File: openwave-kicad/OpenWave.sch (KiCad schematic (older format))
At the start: 38 parts, among them IC1 STM32F405RGT, J1 USB_OTG, J2 503182-1852, SW1 SW_Push, Y1 8MHz, Y2 32.768KHz

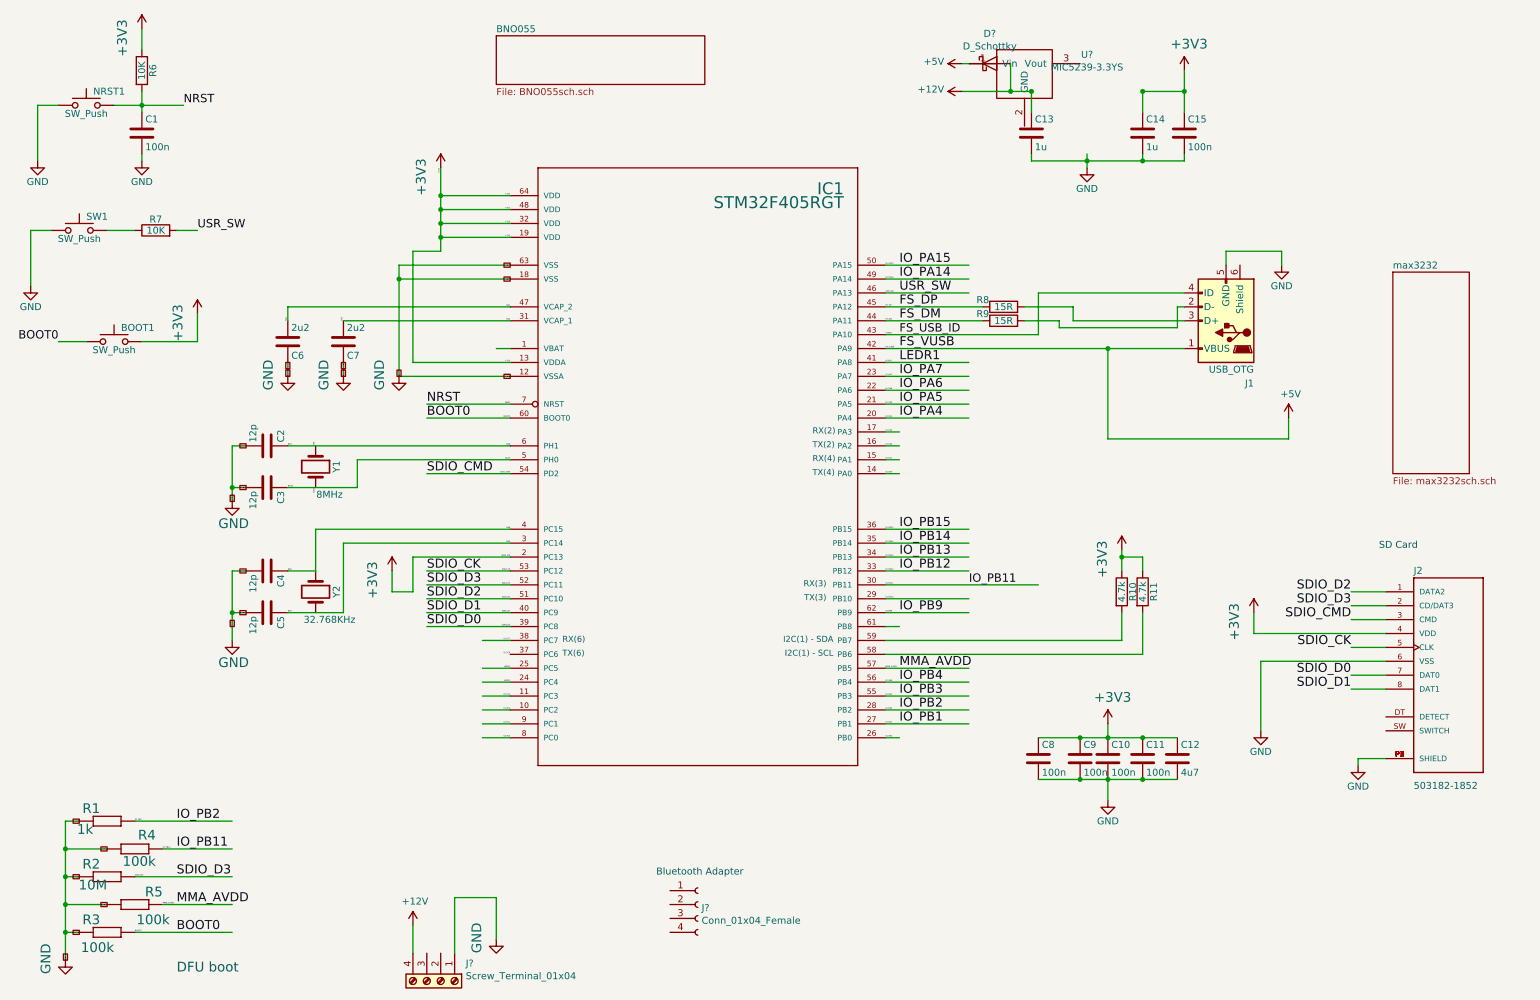
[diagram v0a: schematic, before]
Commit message: finished max232 schematic
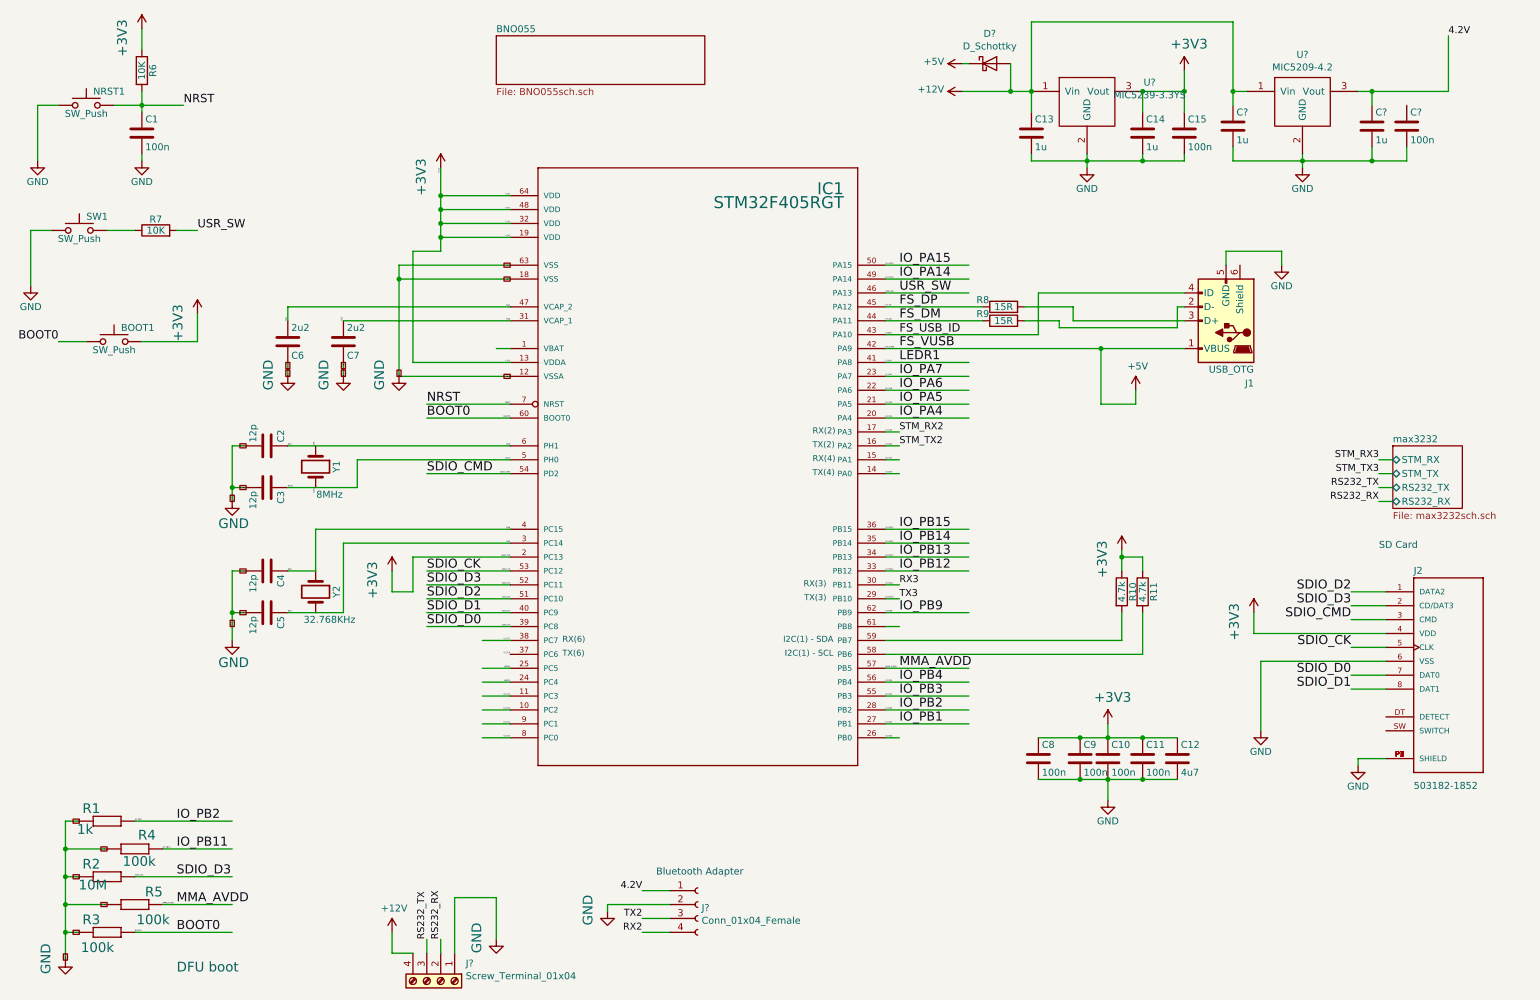
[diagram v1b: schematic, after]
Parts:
- added C? (x2): 1u, Capacitors_SMD:C_0603, symbol Device:C
- added C?: 100n, Capacitors_SMD:C_0603, symbol Device:C
- added U?: MIC5209-4.2, symbol wattnotions:MIC5209-4.2
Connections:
- net labels added: 4.2V, RS232_RX, RS232_TX, RX2, RX3, STM_RX2, STM_RX3, STM_TX2, STM_TX3, TX2, TX3
- wire segments 188 -> 217
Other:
- moved on the sheet: U?
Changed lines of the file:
@@
 	1    0    0    -1
 $EndComp
-Text Label 7300 4650 0    60   ~ 0
-IO_PB11
 $Comp
 L wattnotions:503182-1852 J2
@@
 	3800 5650 4000 5650
 Wire Wire Line
-	6700 4750 7300 4750
-Wire Wire Line
-	6700 4650 7800 4650
-Wire Wire Line
 	3800 5750 4000 5750
 Wire Wire Line
@@
 Wire Wire Line
 	7800 2550 8850 2550
-Wire Wire Line
-	6700 2950 8300 2950
 Wire Wire Line
 	9150 2350 9150 2250
@@
 L power:+5V #PWR?
 U 1 1 5CA98EDB
-P 9600 3450
-F 0 "#PWR?" H 9600 3300 50  0001 C CNN
-F 1 "+5V" H 9615 3623 50  0000 C CNN
-F 2 "" H 9600 3450 50  0001 C CNN
-F 3 "" H 9600 3450 50  0001 C CNN
-	1    9600 3450
-	1    0    0    -1
-$EndComp
-Wire Wire Line
-	8300 2950 8300 3600
-Wire Wire Line
-	8300 3600 9600 3600
-Wire Wire Line
-	9600 3600 9600 3450
-Connection ~ 8300 2950
-Wire Wire Line
-	8300 2950 8850 2950
+P 8500 3250
+F 0 "#PWR?" H 8500 3100 50  0001 C CNN
+F 1 "+5V" H 8515 3423 50  0000 C CNN
+F 2 "" H 8500 3250 50  0001 C CNN
+F 3 "" H 8500 3250 50  0001 C CNN
+	1    8500 3250
+	1    0    0    -1
+$EndComp
 $Comp
 L wattnotions:MIC5239-3.3YS U?
 U 1 1 5CAAC9EC
-P 8150 1000
-F 0 "U?" H 8150 1165 50  0000 C CNN
-F 1 "MIC5239-3.3YS" H 8150 1074 50  0000 C CNN
-F 2 "" H 8150 950 50  0001 C CNN
-F 3 "" H 8150 950 50  0001 C CNN
-	1    8150 1000
+P 8600 1200
+F 0 "U?" H 8600 1365 50  0000 C CNN
+F 1 "MIC5239-3.3YS" H 8600 1274 50  0000 C CNN
+F 2 "" H 8600 1150 50  0001 C CNN
+F 3 "" H 8600 1150 50  0001 C CNN
+	1    8600 1200
 	1    0    0    -1
 $EndComp
@@
 L power:+12V #PWR?
 U 1 1 5CB01041
-P 3300 7100
-F 0 "#PWR?" H 3300 6950 50  0001 C CNN
-F 1 "+12V" H 3315 7273 50  0000 C CNN
-F 2 "" H 3300 7100 50  0001 C CNN
-F 3 "" H 3300 7100 50  0001 C CNN
-	1    3300 7100
+P 3150 7150
+F 0 "#PWR?" H 3150 7000 50  0001 C CNN
+F 1 "+12V" H 3165 7323 50  0000 C CNN
+F 2 "" H 3150 7150 50  0001 C CNN
+F 3 "" H 3150 7150 50  0001 C CNN
+	1    3150 7150
 	1    0    0    -1
 $EndComp
@@
 Wire Wire Line
 	3900 6900 3900 7200
-Wire Wire Line
-	3300 7300 3300 7100
-$Sheet
-S 10350 2400 550  1450
-U 5CB14458
-F0 "max3232" 50
-F1 "max3232sch.sch" 50
-$EndSheet
 Connection ~ 8100 5750
 Wire Wire Line
@@
 Wire Wire Line
 	7250 1100 7600 1100
+$Comp
+L wattnotions:MIC5209-4.2 U?
+U 1 1 5CB69853
+P 9700 1150
+F 0 "U?" H 9700 1465 50  0000 C CNN
+F 1 "MIC5209-4.2" H 9700 1374 50  0000 C CNN
+F 2 "" H 9700 1150 50  0001 C CNN
+F 3 "" H 9700 1150 50  0001 C CNN
+	1    9700 1150
+	1    0    0    -1
+$EndComp
+Wire Wire Line
+	7750 1100 7750 600
+Wire Wire Line
+	7750 600  9200 600
+Wire Wire Line
+	9200 600  9200 1100
+Wire Wire Line
+	9200 1100 9300 1100
+$Comp
+L power:GND #PWR?
+U 1 1 5CB73D5D
+P 9700 1650
+F 0 "#PWR?" H 9700 1400 50  0001 C CNN
+F 1 "GND" H 9700 1500 50  0000 C CNN
+F 2 "" H 9700 1650 50  0001 C CNN
+F 3 "" H 9700 1650 50  0001 C CNN
+	1    9700 1650
+	1    0    0    -1
+$EndComp
+Wire Wire Line
+	9700 1550 9700 1600
+$Comp
+L Device:C C?
+U 1 1 5CB7E204
+P 10200 1350
+F 0 "C?" H 10225 1450 50  0000 L CNN
+F 1 "1u" H 10225 1250 50  0000 L CNN
+F 2 "Capacitors_SMD:C_0603" H 10238 1200 50  0001 C CNN
+F 3 "" H 10200 1350 50  0001 C CNN
+	1    10200 1350
+	1    0    0    -1
+$EndComp
+$Comp
+L Device:C C?
+U 1 1 5CB7E28A
+P 10450 1350
+F 0 "C?" H 10475 1450 50  0000 L CNN
+F 1 "100n" H 10475 1250 50  0000 L CNN
+F 2 "Capacitors_SMD:C_0603" H 10488 1200 50  0001 C CNN
+F 3 "" H 10450 1350 50  0001 C CNN
+	1    10450 1350
+	1    0    0    -1
+$EndComp
+Wire Wire Line
+	10100 1100 10200 1100
+Wire Wire Line
+	10200 1100 10200 1200
+Connection ~ 10200 1100
+Wire Wire Line
+	10200 1100 10750 1100
+Wire Wire Line
+	10200 1500 10200 1600
+Wire Wire Line
+	10200 1600 9700 1600
+Connection ~ 9700 1600
+Wire Wire Line
+	9700 1600 9700 1650
+Wire Wire Line
+	10450 1500 10450 1600
+Wire Wire Line
+	10450 1600 10200 1600
+Connection ~ 10200 1600
+Text Label 10750 700  0    50   ~ 0
+4.2V
+Wire Wire Line
+	10750 700  10750 1100
+$Comp
+L Device:C C?
+U 1 1 5CBB4DA7
+P 9200 1350
+F 0 "C?" H 9225 1450 50  0000 L CNN
+F 1 "1u" H 9225 1250 50  0000 L CNN
+F 2 "Capacitors_SMD:C_0603" H 9238 1200 50  0001 C CNN
+F 3 "" H 9200 1350 50  0001 C CNN
+	1    9200 1350
+	1    0    0    -1
+$EndComp
+Wire Wire Line
+	9200 1100 9200 1200
+Connection ~ 9200 1100
+Wire Wire Line
+	9200 1500 9200 1600
+Wire Wire Line
+	9200 1600 9700 1600
+Text Label 4950 6850 2    50   ~ 0
+4.2V
+Wire Wire Line
+	5150 6850 4950 6850
+Wire Wire Line
+	5150 6950 4700 6950
+Wire Wire Line
+	4700 6950 4700 7000
+$Comp
+L power:GND #GND?
+U 1 1 5CBE31E3
+P 4700 7000
+F 0 "#GND?" H 4600 6900 70  0001 L BNN
+F 1 "GND" V 4600 6900 70  0000 L BNN
+F 2 "" H 4700 7000 60  0001 C CNN
+F 3 "" H 4700 7000 60  0001 C CNN
+	1    4700 7000
+	1    0    0    -1
+$EndComp
+Text Label 6800 3550 0    50   ~ 0
+STM_RX2
+Text Label 6800 3650 0    50   ~ 0
+STM_TX2
+Text Label 4950 7150 2    50   ~ 0
+RX2
+Text Label 4950 7050 2    50   ~ 0
+TX2
+Wire Wire Line
+	4950 7050 5150 7050
+Wire Wire Line
+	4950 7150 5150 7150
+Wire Wire Line
+	6700 2950 8250 2950
+Wire Wire Line
+	8250 2950 8250 3350
+Wire Wire Line
+	8250 3350 8500 3350
+Wire Wire Line
+	8500 3350 8500 3250
+Connection ~ 8250 2950
+Wire Wire Line
+	8250 2950 8850 2950
+Wire Wire Line
+	6700 4750 6800 4750
+Wire Wire Line
+	6700 4650 6800 4650
+Text Label 6800 4650 0    50   ~ 0
+RX3
+Text Label 6800 4750 0    50   ~ 0
+TX3
+Wire Wire Line
+	10350 3750 10250 3750
+Wire Wire Line
+	10350 3850 10250 3850
+Text Label 10250 3750 2    50   ~ 0
+STM_RX3
+Text Label 10250 3850 2    50   ~ 0
+STM_TX3
+$Sheet
+S 10350 3650 500  450
+U 5CB14458
+F0 "max3232" 50
+F1 "max3232sch.sch" 50
+F2 "STM_RX" B L 10350 3750 50
+F3 "STM_TX" B L 10350 3850 50
+F4 "RS232_TX" B L 10350 3950 50
+F5 "RS232_RX" B L 10350 4050 50
+$EndSheet
+Wire Wire Line
+	10350 3950 10250 3950
+Wire Wire Line
+	10350 4050 10250 4050
+Text Label 10250 3950 2    50   ~ 0
+RS232_TX
+Text Label 10250 4050 2    50   ~ 0
+RS232_RX
+Text Label 3400 7200 1    50   ~ 0
+RS232_TX
+Text Label 3500 7200 1    50   ~ 0
+RS232_RX
+Wire Wire Line
+	3300 7300 3150 7300
+Wire Wire Line
+	3150 7300 3150 7150
+Wire Wire Line
+	3400 7300 3400 7200
+Wire Wire Line
+	3500 7300 3500 7200
 $EndSCHEMATC

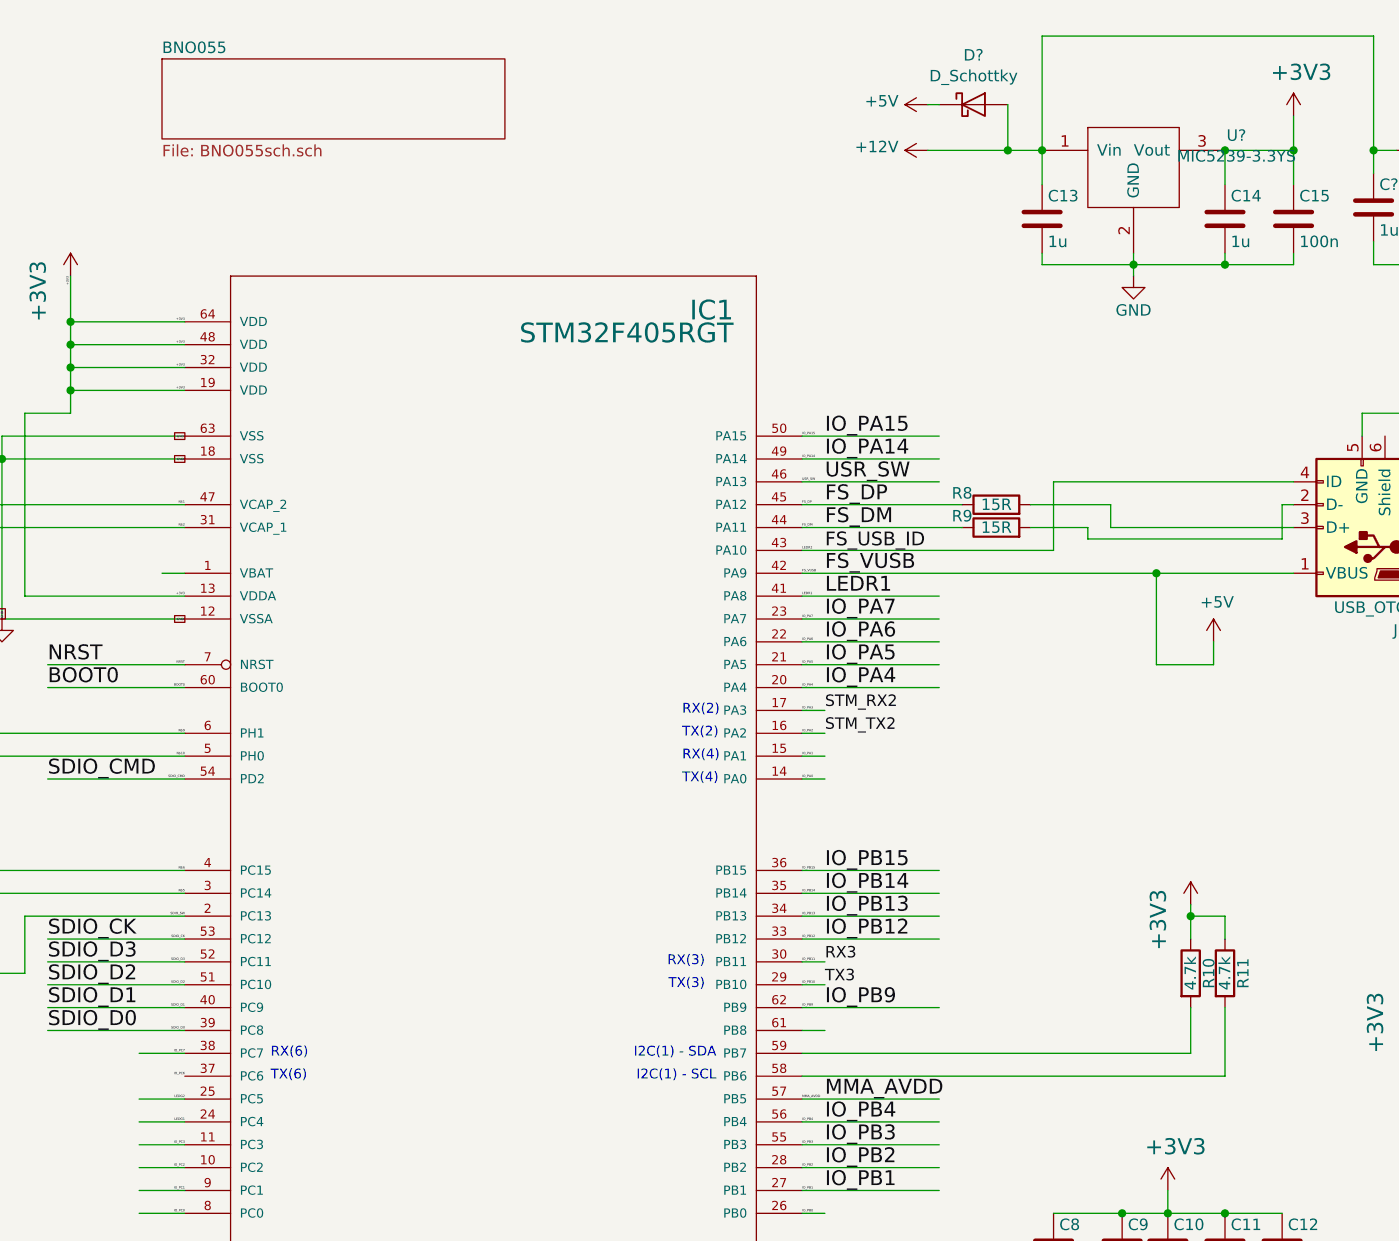
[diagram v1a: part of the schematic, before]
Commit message: finished bno055 schematic
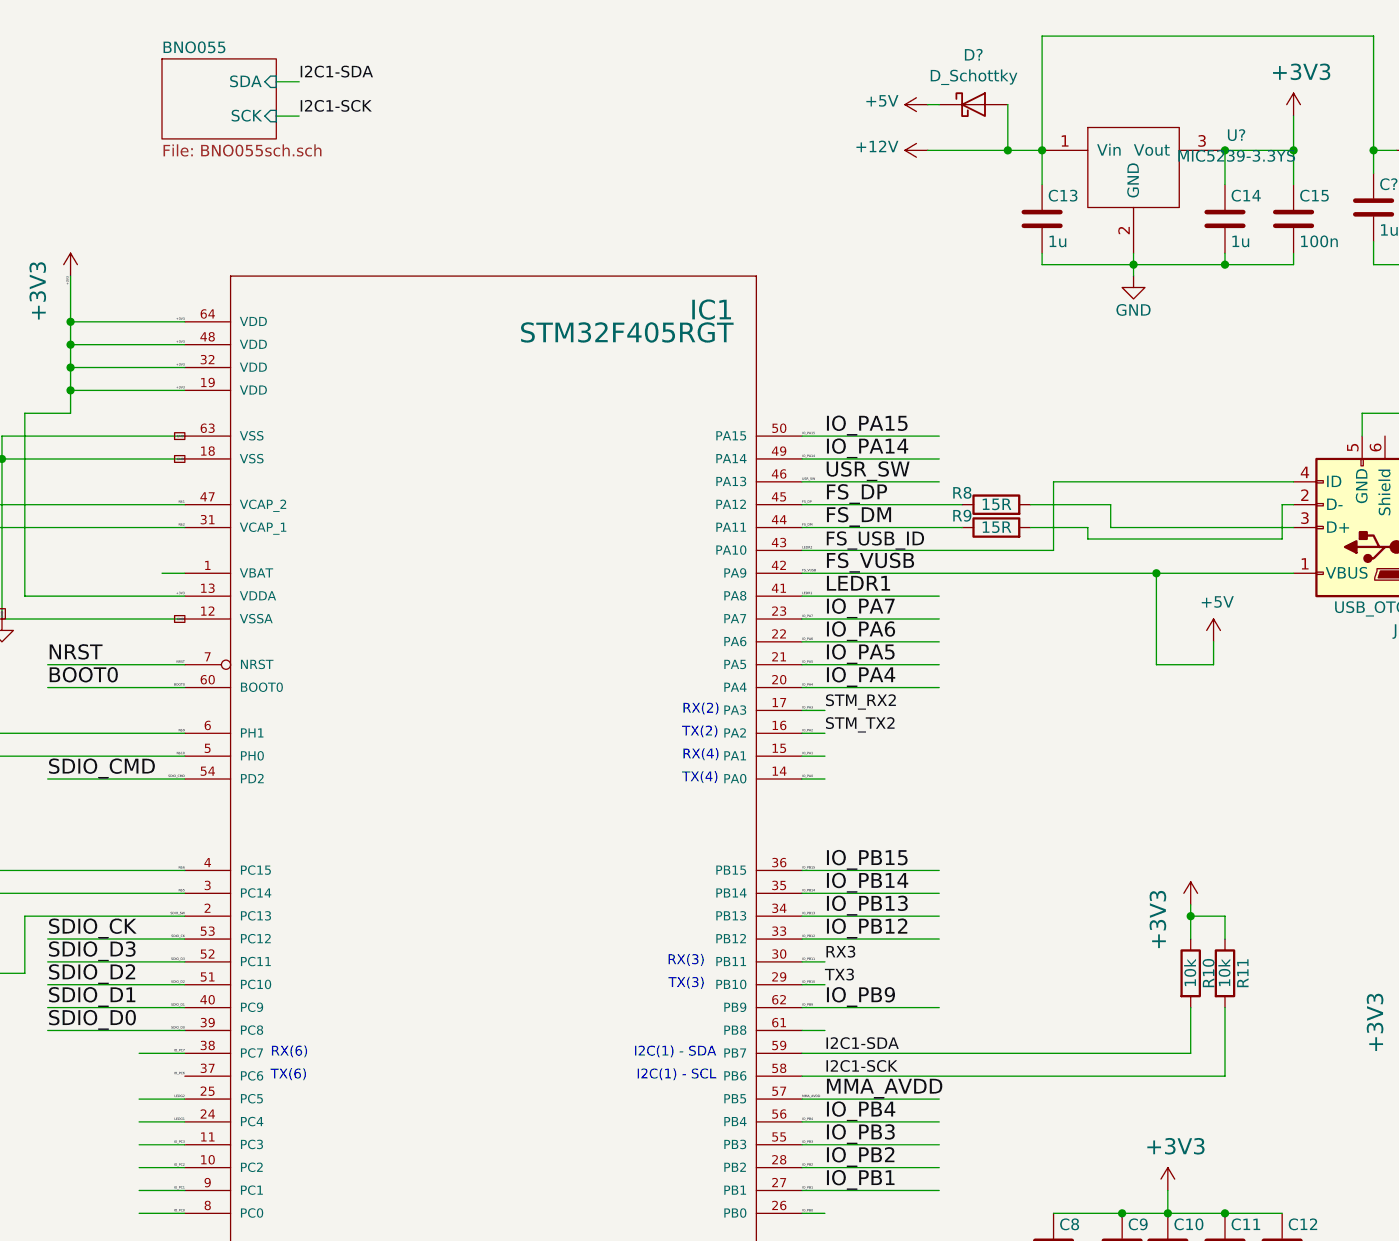
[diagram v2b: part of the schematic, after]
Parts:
- R10, R11: value 4.7k -> 10k
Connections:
- net labels added: I2C1-SCK, I2C1-SDA
- wire segments 217 -> 219
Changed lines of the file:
@@
 P 8400 4700
 F 0 "R10" V 8480 4700 50  0000 C CNN
-F 1 "4.7k" V 8400 4700 50  0000 C CNN
+F 1 "10k" V 8400 4700 50  0000 C CNN
 F 2 "Resistors_SMD:R_0603" V 8330 4700 50  0001 C CNN
 F 3 "" H 8400 4700 50  0001 C CNN
@@
 P 8550 4700
 F 0 "R11" V 8630 4700 50  0000 C CNN
-F 1 "4.7k" V 8550 4700 50  0000 C CNN
+F 1 "10k" V 8550 4700 50  0000 C CNN
 F 2 "Resistors_SMD:R_0603" V 8480 4700 50  0001 C CNN
 F 3 "" H 8550 4700 50  0001 C CNN
@@
 $EndComp
 $Sheet
-S 3900 700  1500 350
+S 3900 700  500  350
 U 5CAE4987
 F0 "BNO055" 50
 F1 "BNO055sch.sch" 50
+F2 "SDA" I R 4400 800 50
+F3 "SCK" I R 4400 950 50
 $EndSheet
 $Comp
@@
 Wire Wire Line
 	3500 7300 3500 7200
+Text Label 6800 5050 0    50   ~ 0
+I2C1-SDA
+Text Label 6800 5150 0    50   ~ 0
+I2C1-SCK
+Text Label 4500 800  0    50   ~ 0
+I2C1-SDA
+Text Label 4500 950  0    50   ~ 0
+I2C1-SCK
+Wire Wire Line
+	4400 800  4500 800
+Wire Wire Line
+	4400 950  4500 950
 $EndSCHEMATC
